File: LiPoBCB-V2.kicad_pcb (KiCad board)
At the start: 2 copper layers, 16 parts, among them J1 USB_C_Receptacle_USB2.0, U1 ETA9740

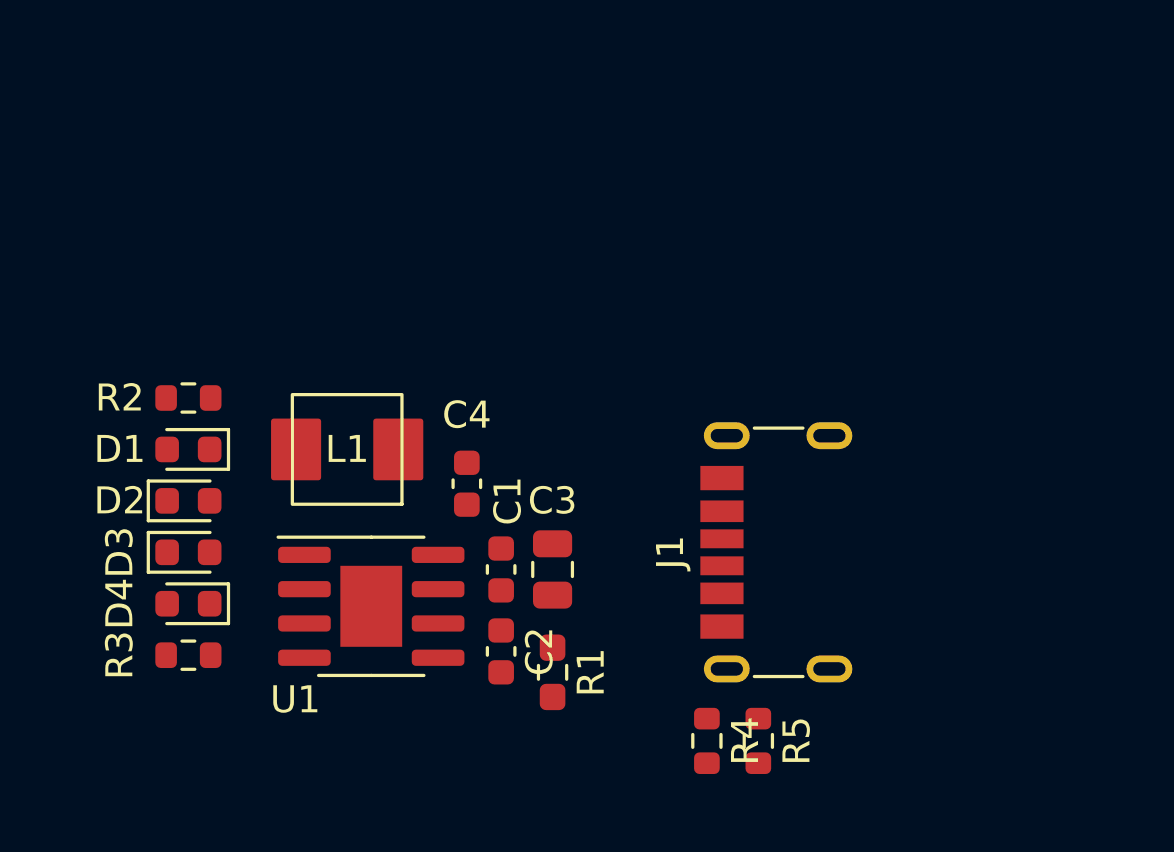
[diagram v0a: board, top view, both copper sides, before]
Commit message: added fets
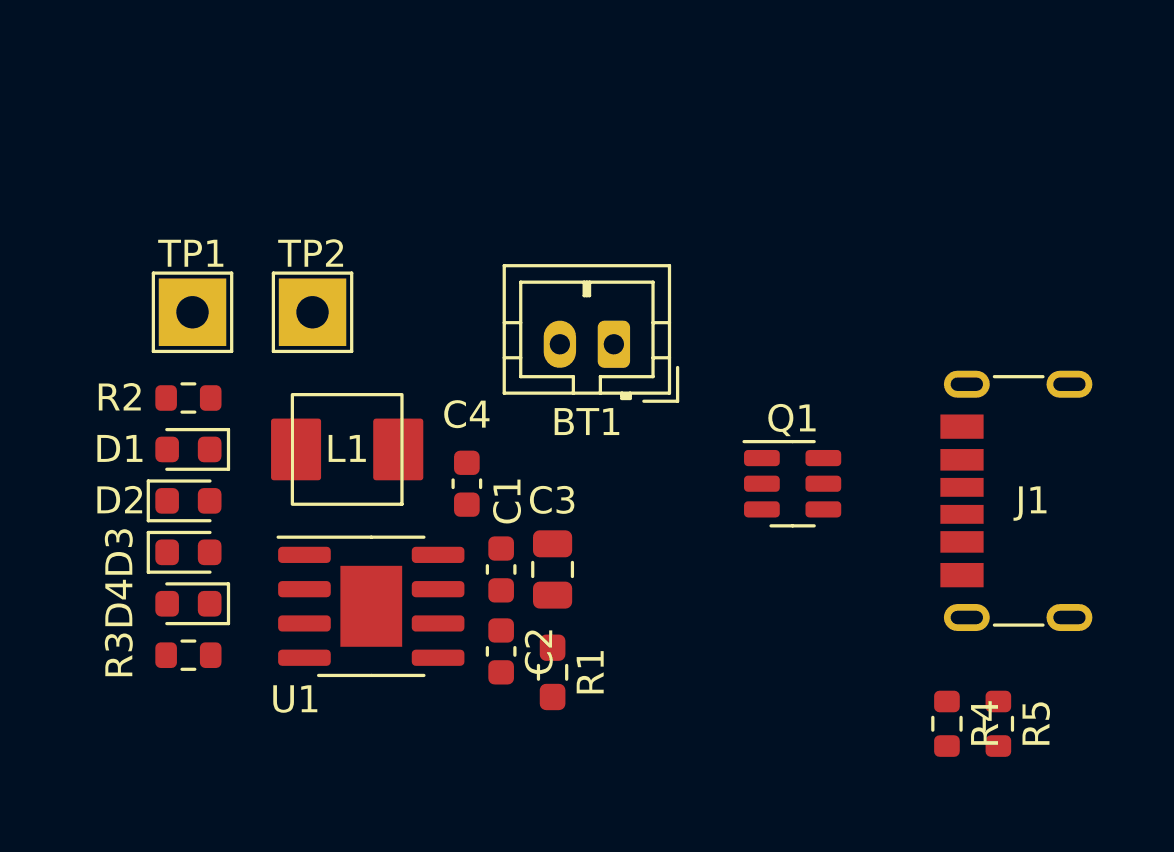
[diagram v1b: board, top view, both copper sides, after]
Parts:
- added BT1: Battery_Cell, Connector_JST:JST_PH_B2B-PH-K_1x02_P2.00mm_Vertical, F.Cu at (160.4, 83.7)
- added Q1: Q_Dual_PMOS_S1G1D2S2G2D1, Package_TO_SOT_SMD:SOT-23-6, F.Cu at (167.0, 88.9)
- added TP1: 5V, TestPoint:TestPoint_THTPad_2.5x2.5mm_Drill1.2mm, F.Cu at (144.8, 82.5)
- added TP2: GND, TestPoint:TestPoint_THTPad_2.5x2.5mm_Drill1.2mm, F.Cu at (149.2, 82.5)
- moved J1 9.09 mm to (173.3, 89.5)
- moved R4 8.91 mm to (172.7, 97.8)
- moved R5 8.91 mm to (174.6, 97.8)
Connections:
- J1 pad A12: (no net) -> GND

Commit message: replaced usb-c port
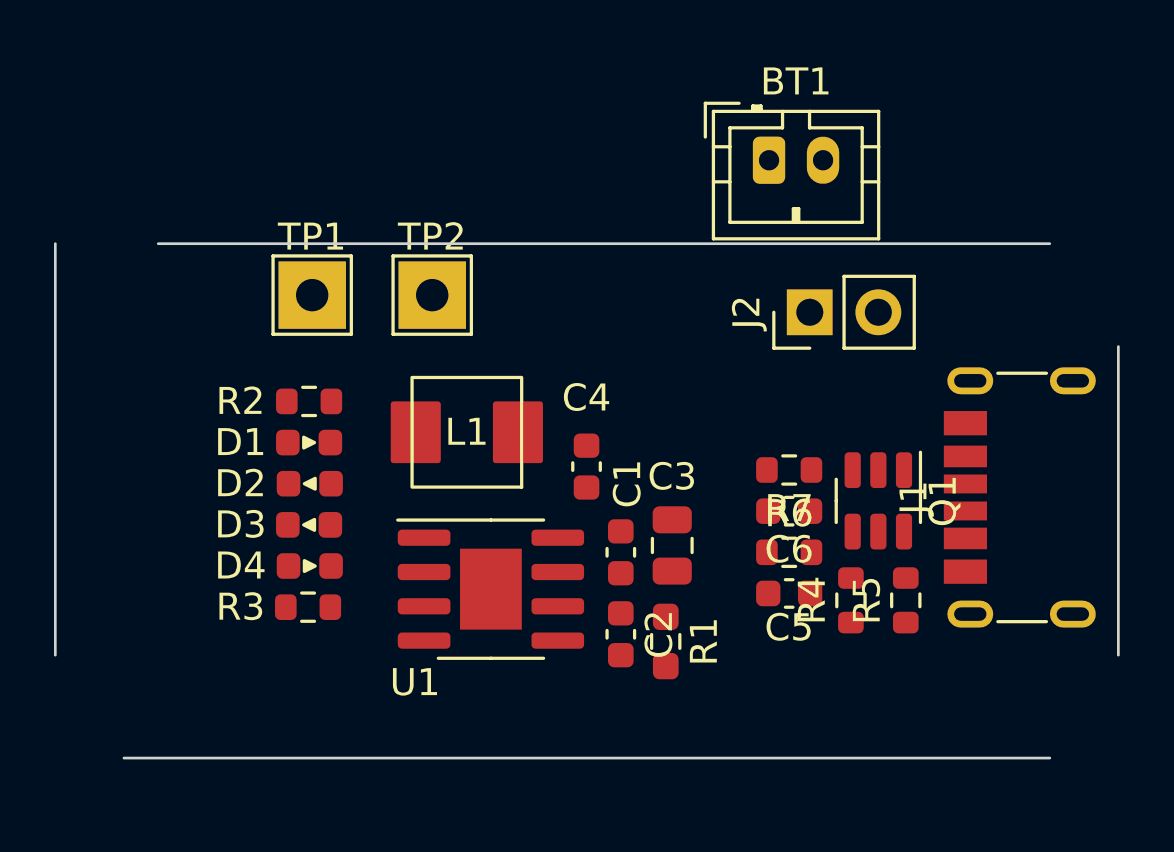
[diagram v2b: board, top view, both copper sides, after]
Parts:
- added C5: 100n, Capacitor_SMD:C_0603_1608Metric, F.Cu at (166.9, 93.0)
- added C6: 100n, Capacitor_SMD:C_0603_1608Metric, F.Cu at (166.9, 89.9)
- added J2: Conn_01x02, Connector_PinHeader_2.54mm:PinHeader_1x02_P2.54mm_Vertical, F.Cu at (167.6, 82.5)
- added R6: 100K, Resistor_SMD:R_0603_1608Metric, F.Cu at (166.9, 91.4)
- added R7: 10K, Resistor_SMD:R_0603_1608Metric, F.Cu at (166.9, 88.4)
- D1, D2, D3, D4: footprint Diode_SMD:D_0603_1608Metric -> LiPoBCB-V2:D_0603_1608Metric
- J1: value USB_C_Receptacle_USB2.0 -> USB-C_6_pin_receptacle
- moved BT1 8.91 mm to (166.1, 76.9), turned to 0 degrees
- moved R4 5.79 mm to (169.2, 93.2), turned to 90 degrees
- moved R5 5.72 mm to (171.2, 93.2), turned to 90 degrees
- moved R3 4.78 mm to (149.1, 93.5)
- moved D4 4.71 mm to (149.1, 91.9)
- moved D3 4.58 mm to (149.1, 90.4)
- moved D2 4.54 mm to (149.1, 88.9)
- moved C3 4.52 mm to (162.5, 91.2)
- moved D1 4.48 mm to (149.1, 87.4)
- moved C4 4.48 mm to (159.4, 88.3)
- moved L1 4.48 mm to (154.9, 87.0)
- moved TP1 4.48 mm to (149.2, 81.9)
- moved TP2 4.48 mm to (153.7, 81.9)
- moved C1 4.48 mm to (160.6, 91.4)
- moved C2 4.48 mm to (160.6, 94.5)
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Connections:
- J1 pad A9: +5V -> /VBUS
- J1 pad B9: +5V -> /VBUS
- Q1 pad 1: Net-(Q1-Pad1) -> /SW_GATE
- Q1 pad 2: unconnected-(Q1-Pad2) -> Net-(C5-Pad1)
- Q1 pad 3: unconnected-(Q1-Pad3) -> /SW_GATE
- Q1 pad 4: unconnected-(Q1-Pad4) -> +5V
- Q1 pad 5: Net-(Q1-Pad1) -> Net-(C5-Pad1)
- Q1 pad 6: Net-(Q1-Pad1) -> /VBUS
- TP1 pad 1: unconnected-(TP1-Pad1) -> +5V
- TP2 pad 1: unconnected-(TP2-Pad1) -> GND
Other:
- board outline added: 39.4 x 19 mm

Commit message: created board outline
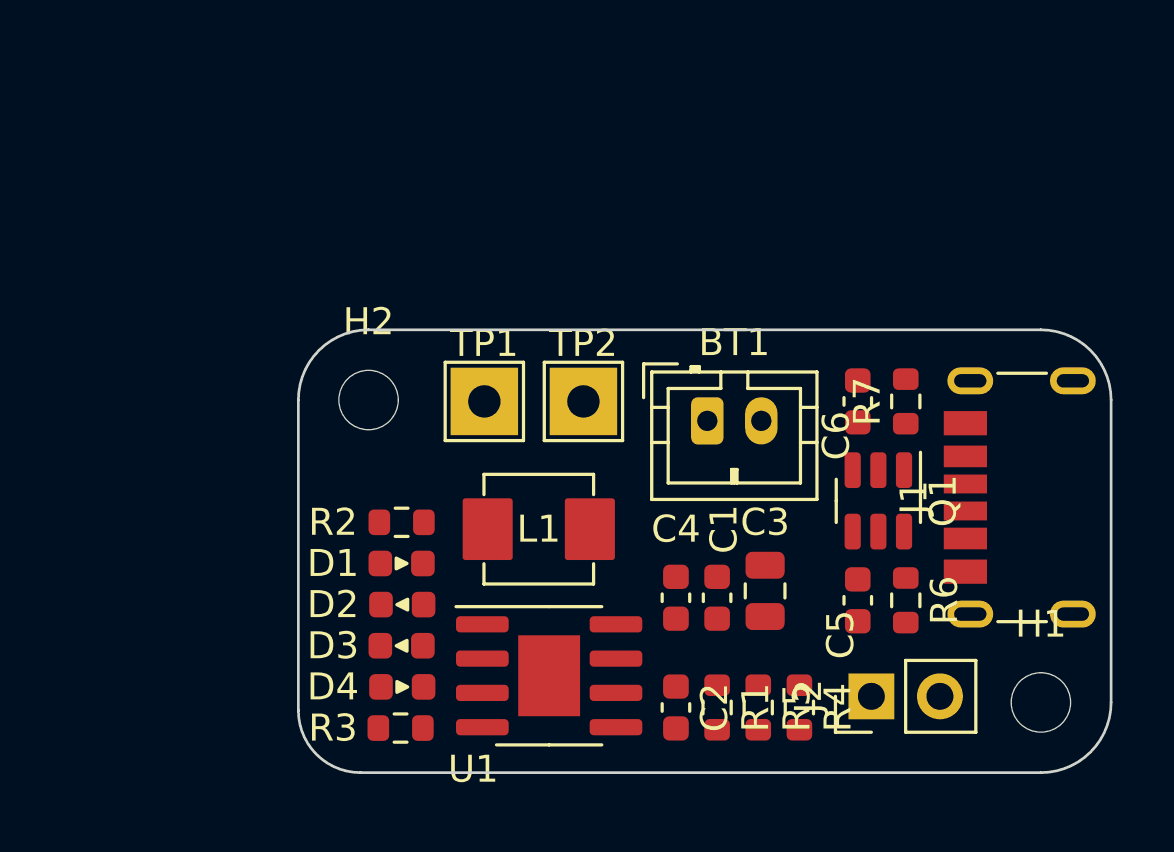
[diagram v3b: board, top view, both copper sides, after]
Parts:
- added H1: MountingHole, MountingHole:MountingHole_2.2mm_M2_ISO14580, F.Cu at (176.2, 97.0)
- added H2: MountingHole, MountingHole:MountingHole_2.2mm_M2_ISO14580, F.Cu at (151.3, 85.8)
- R1: footprint Resistor_SMD:R_0603_1608Metric_Pad0.98x0.95mm_HandSolder -> Resistor_SMD:R_0603_1608Metric
- moved J2 14.4 mm to (169.9, 96.8)
- moved BT1 9.92 mm to (163.8, 86.6)
- moved TP1 7.49 mm to (155.6, 85.9)
- moved TP2 6.85 mm to (159.3, 85.9)
- moved R5 6.75 mm to (165.7, 97.2), turned to -90 degrees
- moved C4 5.88 mm to (162.7, 93.1)
- moved D4 5.64 mm to (152.5, 96.4)
- moved R3 5.64 mm to (152.5, 97.9)
- moved D1 5.64 mm to (152.5, 91.9)
- moved D2 5.64 mm to (152.5, 93.4)
- moved D3 5.64 mm to (152.5, 94.9)
- moved R2 5.64 mm to (152.5, 90.3)
- moved R7 5.01 mm to (171.2, 85.9), turned to 90 degrees
- moved C6 4.79 mm to (169.4, 85.9), turned to 90 degrees
- moved R6 4.67 mm to (171.2, 93.2), turned to -90 degrees
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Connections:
- TP1 pad 1: +5V -> /VBUS
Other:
- board size 39.4 x 19 mm -> 30.1 x 16.4 mm

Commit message: first routing test
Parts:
- moved TP1 3.93 mm to (159.5, 86.1)
- moved TP2 3.31 mm to (156.0, 86.1)
- moved C4 1.68 mm to (161.8, 91.7)
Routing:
- net GND: track 0.00 -> 49.8 mm
- net /BAT: track 0.00 -> 16.9 mm, vias 0 -> 2
- net Net-(C6-Pad2): track 0.00 -> 15.1 mm, vias 0 -> 1
- net /SW_GATE: track 0.00 -> 14.9 mm, vias 0 -> 2
- net +5V: track 0.00 -> 10.7 mm
- net /LED2: track 0.00 -> 7.52 mm
- net /VBUS: track 0.00 -> 6.38 mm
- net /LED1: track 0.00 -> 6.37 mm
- net Net-(C5-Pad1): track 0.00 -> 5.67 mm
- net Net-(D1-Pad1): track 0.00 -> 3.78 mm
- net /SW: track 0.00 -> 3.61 mm
- net Net-(D3-Pad1): track 0.00 -> 3.10 mm
- net /LED3: track 0.00 -> 2.22 mm
